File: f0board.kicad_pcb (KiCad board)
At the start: 2 copper layers, 31 x 18.3 mm, 28 parts, among them P1 CONN_12, P2 CONN_12, SW1 SW_PUSH, U1 STM32F303CCT6, U2 MCP1700, U3 MAX3051, X1 XTAL-SMD-4-PADS

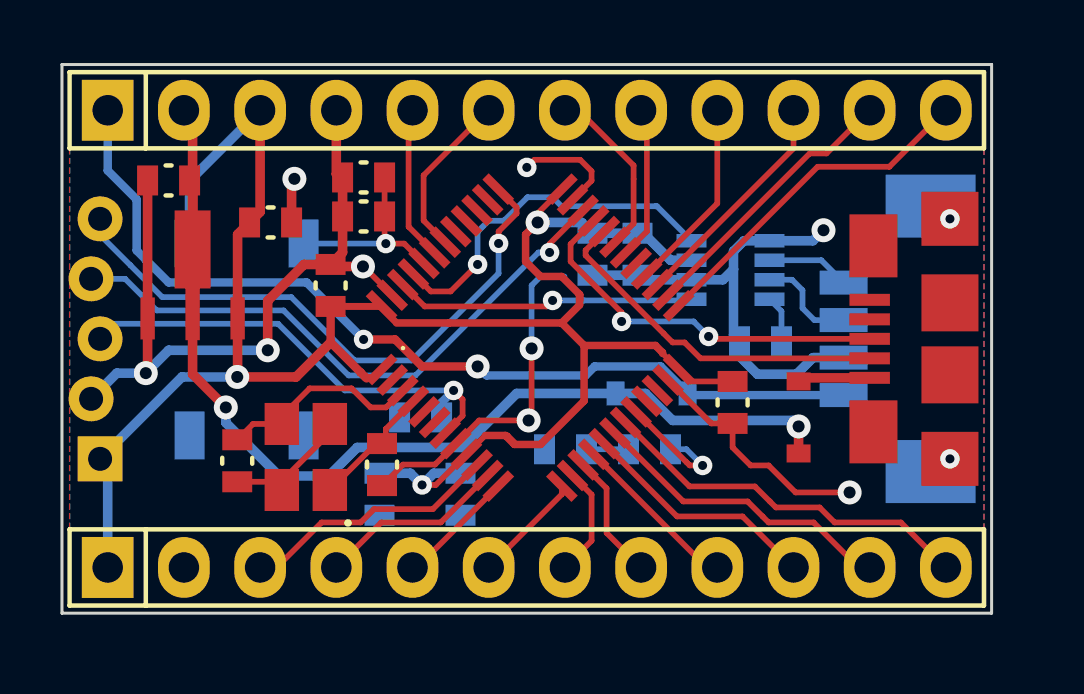
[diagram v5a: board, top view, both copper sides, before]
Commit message: Change dimmension to nicer mm values.
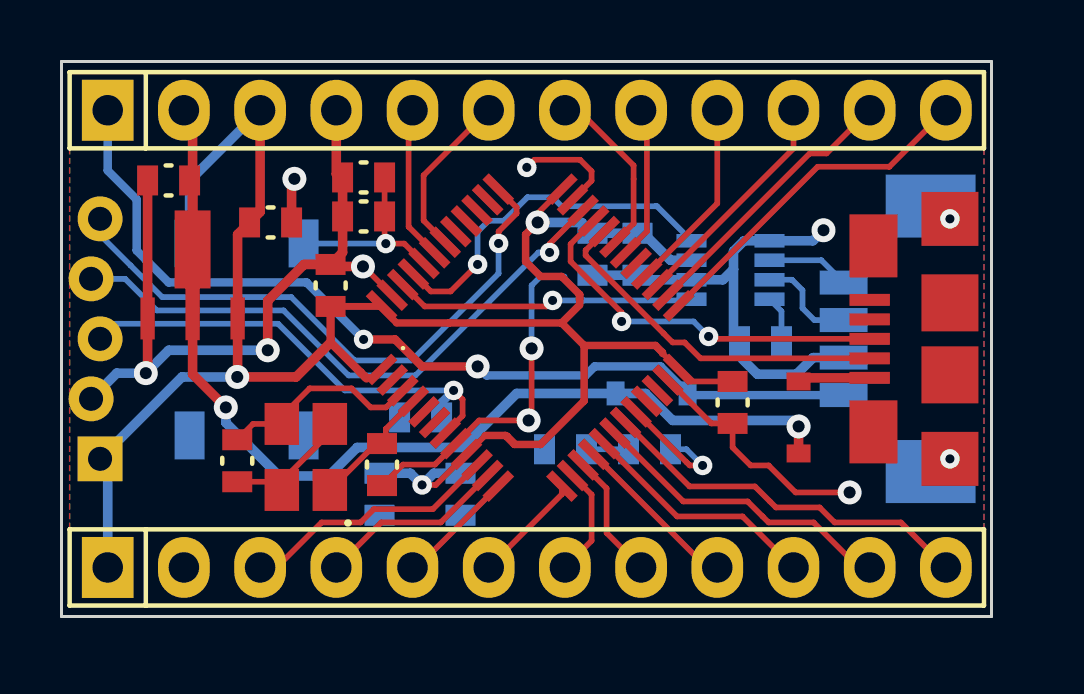
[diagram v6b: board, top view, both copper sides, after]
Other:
- board size 31 x 18.3 mm -> 31 x 18.5 mm
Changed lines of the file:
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@@
       (net 16 /USB_DP) (solder_mask_margin 0.15) (clearance 0.24))
   )
+  (dimension 18.5 (width 0.25) (layer Cmts.User)
+    (gr_text "18.500 mm" (at 21.5 33.025 90) (layer Cmts.User)
+      (effects (font (size 1 1) (thickness 0.25)))
+    )
+    (feature1 (pts (xy 26.4 23.775) (xy 20.5 23.775)))
+    (feature2 (pts (xy 26.4 42.275) (xy 20.5 42.275)))
+    (crossbar (pts (xy 22.5 42.275) (xy 22.5 23.775)))
+    (arrow1a (pts (xy 22.5 23.775) (xy 23.086421 24.901504)))
+    (arrow1b (pts (xy 22.5 23.775) (xy 21.913579 24.901504)))
+    (arrow2a (pts (xy 22.5 42.275) (xy 23.086421 41.148496)))
+    (arrow2b (pts (xy 22.5 42.275) (xy 21.913579 41.148496)))
+  )
+  (dimension 31 (width 0.25) (layer Cmts.User)
+    (gr_text "31.000 mm" (at 41.9 18.7) (layer Cmts.User)
+      (effects (font (size 1 1) (thickness 0.25)))
+    )
+    (feature1 (pts (xy 26.4 23.8) (xy 26.4 17.7)))
+    (feature2 (pts (xy 57.4 23.8) (xy 57.4 17.7)))
+    (crossbar (pts (xy 57.4 19.7) (xy 26.4 19.7)))
+    (arrow1a (pts (xy 26.4 19.7) (xy 27.526504 19.113579)))
+    (arrow1b (pts (xy 26.4 19.7) (xy 27.526504 20.286421)))
+    (arrow2a (pts (xy 57.4 19.7) (xy 56.273496 19.113579)))
+    (arrow2b (pts (xy 57.4 19.7) (xy 56.273496 20.286421)))
+  )
+  (gr_line (start 57.4 23.775) (end 57.4 42.275) (angle 90) (layer Edge.Cuts) (width 0.1))
+  (gr_line (start 26.4 23.775) (end 57.4 23.775) (angle 90) (layer Edge.Cuts) (width 0.1))
+  (gr_line (start 26.4 42.275) (end 26.4 23.775) (angle 90) (layer Edge.Cuts) (width 0.1))
+  (gr_line (start 57.4 42.275) (end 26.4 42.275) (angle 90) (layer Edge.Cuts) (width 0.1))
   (gr_text "1\n2" (at 55.6 26.9 90) (layer B.SilkS)
     (effects (font (size 1 1) (thickness 0.25)) (justify mirror))
@@
     (effects (font (size 1 1) (thickness 0.25)) (justify mirror))
   )
-  (dimension 30.988 (width 0.3) (layer Cmts.User)
-    (gr_text "30.988 mm" (at 41.91 19.478) (layer Cmts.User)
-      (effects (font (size 1.5 1.5) (thickness 0.3)))
-    )
-    (feature1 (pts (xy 57.404 23.876) (xy 57.404 18.128)))
-    (feature2 (pts (xy 26.416 23.876) (xy 26.416 18.128)))
-    (crossbar (pts (xy 26.416 20.828) (xy 57.404 20.828)))
-    (arrow1a (pts (xy 57.404 20.828) (xy 56.277496 21.414421)))
-    (arrow1b (pts (xy 57.404 20.828) (xy 56.277496 20.241579)))
-    (arrow2a (pts (xy 26.416 20.828) (xy 27.542504 21.414421)))
-    (arrow2b (pts (xy 26.416 20.828) (xy 27.542504 20.241579)))
-  )
-  (dimension 18.288 (width 0.3) (layer Cmts.User)
-    (gr_text "18.288 mm" (at 22.272 33.02 90) (layer Cmts.User)
-      (effects (font (size 1.5 1.5) (thickness 0.3)))
-    )
-    (feature1 (pts (xy 26.416 23.876) (xy 20.922 23.876)))
-    (feature2 (pts (xy 26.416 42.164) (xy 20.922 42.164)))
-    (crossbar (pts (xy 23.622 42.164) (xy 23.622 23.876)))
-    (arrow1a (pts (xy 23.622 23.876) (xy 24.208421 25.002504)))
-    (arrow1b (pts (xy 23.622 23.876) (xy 23.035579 25.002504)))
-    (arrow2a (pts (xy 23.622 42.164) (xy 24.208421 41.037496)))
-    (arrow2b (pts (xy 23.622 42.164) (xy 23.035579 41.037496)))
-  )
-  (gr_line (start 26.416 42.164) (end 26.416 23.876) (angle 90) (layer Edge.Cuts) (width 0.1))
-  (gr_line (start 57.404 42.164) (end 26.416 42.164) (angle 90) (layer Edge.Cuts) (width 0.1))
-  (gr_line (start 57.404 23.876) (end 57.404 42.164) (angle 90) (layer Edge.Cuts) (width 0.1))
-  (gr_line (start 26.416 23.876) (end 57.404 23.876) (angle 90) (layer Edge.Cuts) (width 0.1))
   (segment (start 52.472 33.645) (end 51.455 33.645) (width 0.32) (layer B.Cu) (net 1))
   (segment (start 49.6 34.2) (end 49 33.6) (width 0.32) (layer B.Cu) (net 1))
